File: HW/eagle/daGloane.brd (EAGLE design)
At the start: 182.4 x 160.7 mm, 64 parts, among them IC1 MCP1252-33X50, U1 STM32F10XTXU6, X2 SPARKFUN-CONNECTORS_USB-MICROB

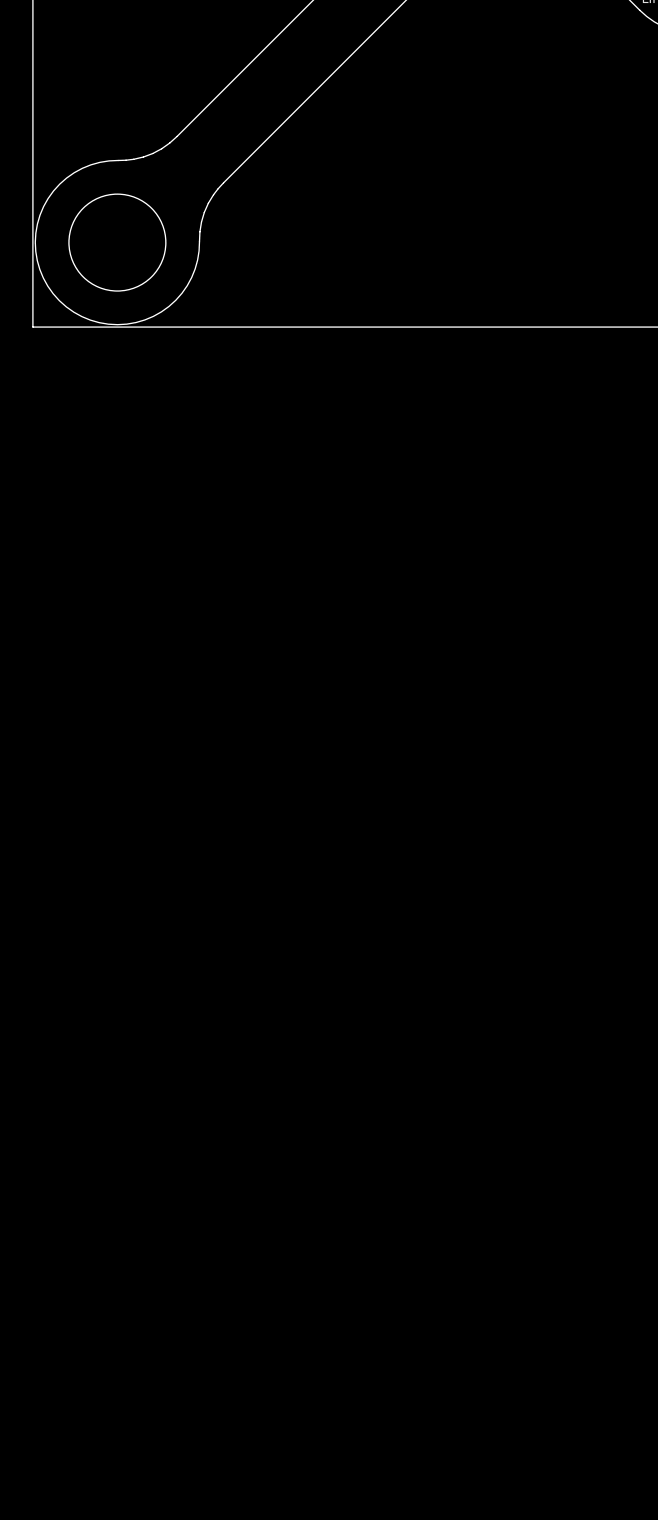
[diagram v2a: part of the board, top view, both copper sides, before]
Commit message: frame with bldc drive version added to schematic
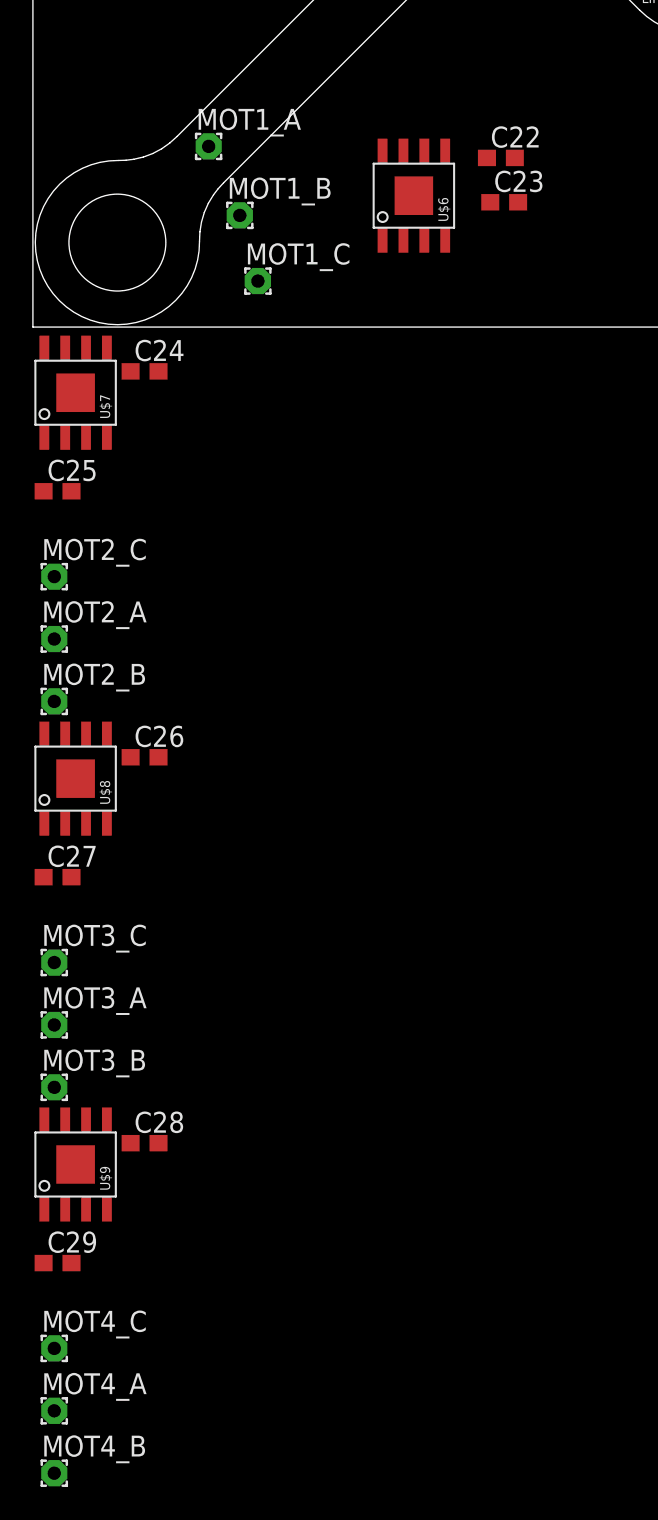
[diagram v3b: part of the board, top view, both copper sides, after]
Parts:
- added C22, C23, C24, C25, C26, C27, C28, C29: 1µF, rcl:C0603
- added MOT1_A, MOT1_B, MOT1_C, MOT2_A, MOT2_B, MOT2_C, MOT3_A, MOT3_B, MOT3_C, MOT4_A, MOT4_B, MOT4_C: WIREPAD1,6/0,8, wirepad:1,6/0,8
- added U$6, U$7, U$8, U$9: MTD6501C, daGloane:SOP-8
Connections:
- new net MOT1_A: MOT1_A.1, U$6.3
- new net MOT1_A1: MOT2_A.1, U$7.3
- new net MOT1_A2: MOT3_A.1, U$8.3
- new net MOT1_A3: MOT4_A.1, U$9.3
- new net N$26: C22.2, U$6.2
- new net N$27: MOT1_B.1, U$6.4
- new net N$29: MOT1_C.1, U$6.6
- new net N$30: MOT2_B.1, U$7.4
- new net N$31: MOT2_C.1, U$7.6
- new net N$32: C24.2, U$7.2
- new net N$33: MOT3_B.1, U$8.4
- new net N$34: MOT3_C.1, U$8.6
- new net N$35: C26.2, U$8.2
- new net N$36: MOT4_B.1, U$9.4
- new net N$37: MOT4_C.1, U$9.6
- new net N$38: C28.2, U$9.2
- new net V_MOT: C23.2, C25.2, C27.2, C29.2, U$6.7, U$7.7, U$8.7, U$9.7
- net GND: now also C22.1, C23.1, C24.1, C25.1, C26.1, C27.1, C28.1, C29.1, U$6.5, U$7.5, U$8.5, U$9.5
- net MOT1: now also U$6.8
- net MOT2: now also U$7.8
- net MOT3: now also U$8.8
- net MOT4: now also U$9.8
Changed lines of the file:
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@@
 <?xml version="1.0" encoding="utf-8"?>
 <!DOCTYPE eagle SYSTEM "eagle.dtd">
-<eagle version="6.2">
+<eagle version="6.1">
 <drawing>
 <settings>
@@
 <attribute name="VALUE" x="23.595" y="32.825" size="0.6096" layer="27"/>
 </element>
+<element name="U$6" library="daGloane" package="SOP-8" value="MTD6501C" x="23.2" y="8"/>
+<element name="C22" library="rcl" package="C0603" value="1µF" x="28.5" y="10.3"/>
+<element name="C23" library="rcl" package="C0603" value="1µF" x="28.7" y="7.6"/>
+<element name="MOT1_A" library="wirepad" package="1,6/0,8" value="WIREPAD1,6/0,8" x="10.7" y="11"/>
+<element name="MOT1_B" library="wirepad" package="1,6/0,8" value="WIREPAD1,6/0,8" x="12.6" y="6.8"/>
+<element name="MOT1_C" library="wirepad" package="1,6/0,8" value="WIREPAD1,6/0,8" x="13.7" y="2.8"/>
+<element name="U$7" library="daGloane" package="SOP-8" value="MTD6501C" x="2.6" y="-4"/>
+<element name="C24" library="rcl" package="C0603" value="1µF" x="6.8" y="-2.7"/>
+<element name="C25" library="rcl" package="C0603" value="1µF" x="1.5" y="-10"/>
+<element name="MOT2_A" library="wirepad" package="1,6/0,8" value="WIREPAD1,6/0,8" x="1.3" y="-19"/>
+<element name="MOT2_B" library="wirepad" package="1,6/0,8" value="WIREPAD1,6/0,8" x="1.3" y="-22.8"/>
+<element name="MOT2_C" library="wirepad" package="1,6/0,8" value="WIREPAD1,6/0,8" x="1.3" y="-15.2"/>
+<element name="U$8" library="daGloane" package="SOP-8" value="MTD6501C" x="2.6" y="-27.5"/>
+<element name="C26" library="rcl" package="C0603" value="1µF" x="6.8" y="-26.2"/>
+<element name="C27" library="rcl" package="C0603" value="1µF" x="1.5" y="-33.5"/>
+<element name="MOT3_A" library="wirepad" package="1,6/0,8" value="WIREPAD1,6/0,8" x="1.3" y="-42.5"/>
+<element name="MOT3_B" library="wirepad" package="1,6/0,8" value="WIREPAD1,6/0,8" x="1.3" y="-46.3"/>
+<element name="MOT3_C" library="wirepad" package="1,6/0,8" value="WIREPAD1,6/0,8" x="1.3" y="-38.7"/>
+<element name="U$9" library="daGloane" package="SOP-8" value="MTD6501C" x="2.6" y="-51"/>
+<element name="C28" library="rcl" package="C0603" value="1µF" x="6.8" y="-49.7"/>
+<element name="C29" library="rcl" package="C0603" value="1µF" x="1.5" y="-57"/>
+<element name="MOT4_A" library="wirepad" package="1,6/0,8" value="WIREPAD1,6/0,8" x="1.3" y="-66"/>
+<element name="MOT4_B" library="wirepad" package="1,6/0,8" value="WIREPAD1,6/0,8" x="1.3" y="-69.8"/>
+<element name="MOT4_C" library="wirepad" package="1,6/0,8" value="WIREPAD1,6/0,8" x="1.3" y="-62.2"/>
 </elements>
 <signals>
@@
 <contactref element="U$5" pad="P$22"/>
 <contactref element="C21" pad="2"/>
+<contactref element="U$6" pad="5"/>
+<contactref element="U$6" pad="5"/>
+<contactref element="C22" pad="1"/>
+<contactref element="C23" pad="1"/>
+<contactref element="U$7" pad="5"/>
+<contactref element="U$7" pad="5"/>
+<contactref element="C24" pad="1"/>
+<contactref element="C25" pad="1"/>
+<contactref element="U$8" pad="5"/>
+<contactref element="U$8" pad="5"/>
+<contactref element="C26" pad="1"/>
+<contactref element="C27" pad="1"/>
+<contactref element="U$9" pad="5"/>
+<contactref element="U$9" pad="5"/>
+<contactref element="C28" pad="1"/>
+<contactref element="C29" pad="1"/>
 <wire x1="91.72993125" y1="23.41184375" x2="94.367440625" y2="24.380578125" width="0" layer="19" extent="16-16"/>
 <wire x1="92.15419375" y1="21.99763125" x2="91.72993125" y2="23.41184375" width="0" layer="19" extent="16-16"/>
@@
 <wire x1="25.95" y1="62" x2="34.7" y2="55.2" width="0" layer="19" extent="1-1"/>
 <wire x1="25.95" y1="66" x2="25.95" y2="62" width="0" layer="19" extent="1-1"/>
+<wire x1="27.65" y1="10.3" x2="33.8" y2="27.55" width="0" layer="19" extent="1-1"/>
+<wire x1="25.105" y1="10.7" x2="27.65" y2="10.3" width="0" layer="19" extent="1-1"/>
+<wire x1="27.85" y1="7.6" x2="27.65" y2="10.3" width="0" layer="19" extent="1-1"/>
+<wire x1="5.95" y1="-2.7" x2="25.105" y2="10.7" width="0" layer="19" extent="1-1"/>
+<wire x1="4.505" y1="-1.3" x2="5.95" y2="-2.7" width="0" layer="19" extent="1-1"/>
+<wire x1="0.65" y1="-10" x2="5.95" y2="-2.7" width="0" layer="19" extent="1-1"/>
+<wire x1="4.505" y1="-24.8" x2="0.65" y2="-10" width="0" layer="19" extent="1-1"/>
+<wire x1="5.95" y1="-26.2" x2="4.505" y2="-24.8" width="0" layer="19" extent="1-1"/>
+<wire x1="0.65" y1="-33.5" x2="5.95" y2="-26.2" width="0" layer="19" extent="1-1"/>
+<wire x1="4.505" y1="-48.3" x2="0.65" y2="-33.5" width="0" layer="19" extent="1-1"/>
+<wire x1="5.95" y1="-49.7" x2="4.505" y2="-48.3" width="0" layer="19" extent="1-1"/>
+<wire x1="0.65" y1="-57" x2="5.95" y2="-49.7" width="0" layer="19" extent="1-1"/>
 </signal>
 <signal name="LED1">
@@
 <signal name="MOT4">
 <contactref element="U1" pad="32"/>
+<contactref element="U$9" pad="8"/>
+<wire x1="0.695" y1="-48.3" x2="40.5" y2="55.375" width="0" layer="19" extent="1-1"/>
 </signal>
 <signal name="N$1">
@@
 <signal name="MOT1">
 <contactref element="U1" pad="15"/>
+<contactref element="U$6" pad="8"/>
+<wire x1="21.295" y1="10.7" x2="41" y2="49.825" width="0" layer="19" extent="1-1"/>
 </signal>
 <signal name="MOT2">
 <contactref element="U1" pad="16"/>
+<contactref element="U$7" pad="8"/>
+<wire x1="0.695" y1="-1.3" x2="41.5" y2="49.825" width="0" layer="19" extent="1-1"/>
 </signal>
 <signal name="MOT3">
 <contactref element="U1" pad="31"/>
+<contactref element="U$8" pad="8"/>
+<wire x1="0.695" y1="-24.8" x2="41" y2="55.375" width="0" layer="19" extent="1-1"/>
+</signal>
+<signal name="MOT1_A">
+<contactref element="U$6" pad="3"/>
+<contactref element="MOT1_A" pad="1"/>
+<wire x1="23.835" y1="5.3" x2="10.7" y2="11" width="0" layer="19" extent="1-1"/>
+</signal>
+<signal name="N$27">
+<contactref element="U$6" pad="4"/>
+<contactref element="MOT1_B" pad="1"/>
+<wire x1="25.105" y1="5.3" x2="12.6" y2="6.8" width="0" layer="19" extent="1-1"/>
+</signal>
+<signal name="N$29">
+<contactref element="U$6" pad="6"/>
+<contactref element="MOT1_C" pad="1"/>
+<wire x1="23.835" y1="10.7" x2="13.7" y2="2.8" width="0" layer="19" extent="1-1"/>
+</signal>
+<signal name="N$26">
+<contactref element="U$6" pad="2"/>
+<contactref element="C22" pad="2"/>
+<wire x1="22.565" y1="5.3" x2="29.35" y2="10.3" width="0" layer="19" extent="1-1"/>
+</signal>
+<signal name="V_MOT">
+<contactref element="U$6" pad="7"/>
+<contactref element="C23" pad="2"/>
+<contactref element="U$7" pad="7"/>
+<contactref element="C25" pad="2"/>
+<contactref element="U$8" pad="7"/>
+<contactref element="C27" pad="2"/>
+<contactref element="U$9" pad="7"/>
+<contactref element="C29" pad="2"/>
+<wire x1="1.965" y1="-48.3" x2="2.35" y2="-57" width="0" layer="19" extent="1-1"/>
+<wire x1="2.35" y1="-33.5" x2="1.965" y2="-48.3" width="0" layer="19" extent="1-1"/>
+<wire x1="1.965" y1="-24.8" x2="2.35" y2="-33.5" width="0" layer="19" extent="1-1"/>
+<wire x1="2.35" y1="-10" x2="1.965" y2="-24.8" width="0" layer="19" extent="1-1"/>
+<wire x1="1.965" y1="-1.3" x2="2.35" y2="-10" width="0" layer="19" extent="1-1"/>
+<wire x1="22.565" y1="10.7" x2="1.965" y2="-1.3" width="0" layer="19" extent="1-1"/>
+<wire x1="29.55" y1="7.6" x2="22.565" y2="10.7" width="0" layer="19" extent="1-1"/>
+</signal>
+<signal name="MOT1_A1">
+<contactref element="U$7" pad="3"/>
+<contactref element="MOT2_A" pad="1"/>
+<wire x1="3.235" y1="-6.7" x2="1.3" y2="-19" width="0" layer="19" extent="1-1"/>
+</signal>
+<signal name="N$30">
+<contactref element="U$7" pad="4"/>
+<contactref element="MOT2_B" pad="1"/>
+<wire x1="4.505" y1="-6.7" x2="1.3" y2="-22.8" width="0" layer="19" extent="1-1"/>
+</signal>
+<signal name="N$31">
+<contactref element="U$7" pad="6"/>
+<contactref element="MOT2_C" pad="1"/>
+<wire x1="3.235" y1="-1.3" x2="1.3" y2="-15.2" width="0" layer="19" extent="1-1"/>
+</signal>
+<signal name="N$32">
+<contactref element="U$7" pad="2"/>
+<contactref element="C24" pad="2"/>
+<wire x1="7.65" y1="-2.7" x2="1.965" y2="-6.7" width="0" layer="19" extent="1-1"/>
+</signal>
+<signal name="MOT1_A2">
+<contactref element="U$8" pad="3"/>
+<contactref element="MOT3_A" pad="1"/>
+<wire x1="3.235" y1="-30.2" x2="1.3" y2="-42.5" width="0" layer="19" extent="1-1"/>
+</signal>
+<signal name="N$33">
+<contactref element="U$8" pad="4"/>
+<contactref element="MOT3_B" pad="1"/>
+<wire x1="4.505" y1="-30.2" x2="1.3" y2="-46.3" width="0" layer="19" extent="1-1"/>
+</signal>
+<signal name="N$34">
+<contactref element="U$8" pad="6"/>
+<contactref element="MOT3_C" pad="1"/>
+<wire x1="3.235" y1="-24.8" x2="1.3" y2="-38.7" width="0" layer="19" extent="1-1"/>
+</signal>
+<signal name="N$35">
+<contactref element="U$8" pad="2"/>
+<contactref element="C26" pad="2"/>
+<wire x1="7.65" y1="-26.2" x2="1.965" y2="-30.2" width="0" layer="19" extent="1-1"/>
+</signal>
+<signal name="MOT1_A3">
+<contactref element="U$9" pad="3"/>
+<contactref element="MOT4_A" pad="1"/>
+<wire x1="3.235" y1="-53.7" x2="1.3" y2="-66" width="0" layer="19" extent="1-1"/>
+</signal>
+<signal name="N$36">
+<contactref element="U$9" pad="4"/>
+<contactref element="MOT4_B" pad="1"/>
+<wire x1="4.505" y1="-53.7" x2="1.3" y2="-69.8" width="0" layer="19" extent="1-1"/>
+</signal>
+<signal name="N$37">
+<contactref element="U$9" pad="6"/>
+<contactref element="MOT4_C" pad="1"/>
+<wire x1="3.235" y1="-48.3" x2="1.3" y2="-62.2" width="0" layer="19" extent="1-1"/>
+</signal>
+<signal name="N$38">
+<contactref element="U$9" pad="2"/>
+<contactref element="C28" pad="2"/>
+<wire x1="7.65" y1="-49.7" x2="1.965" y2="-53.7" width="0" layer="19" extent="1-1"/>
 </signal>
 </signals>

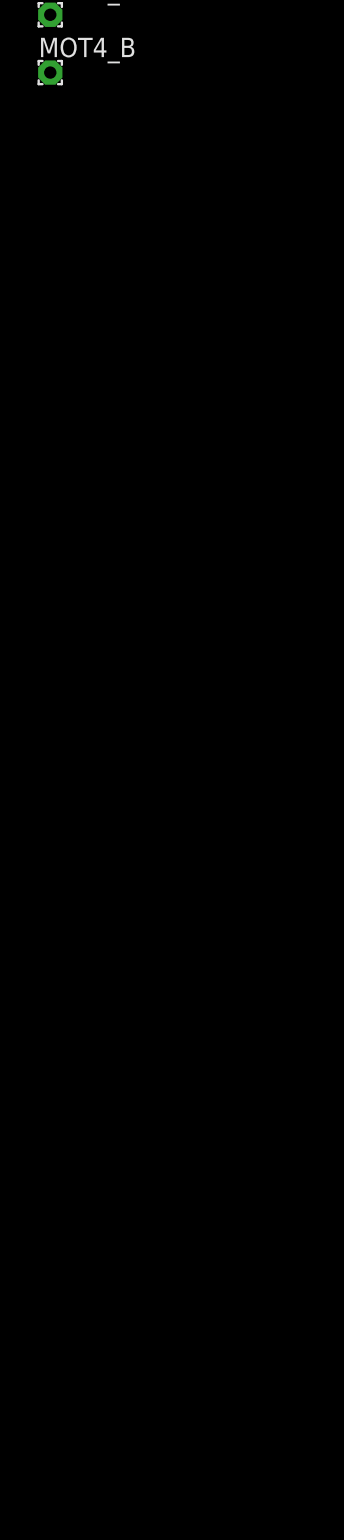
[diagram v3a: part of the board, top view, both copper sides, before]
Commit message: DC motor drive added to schematic
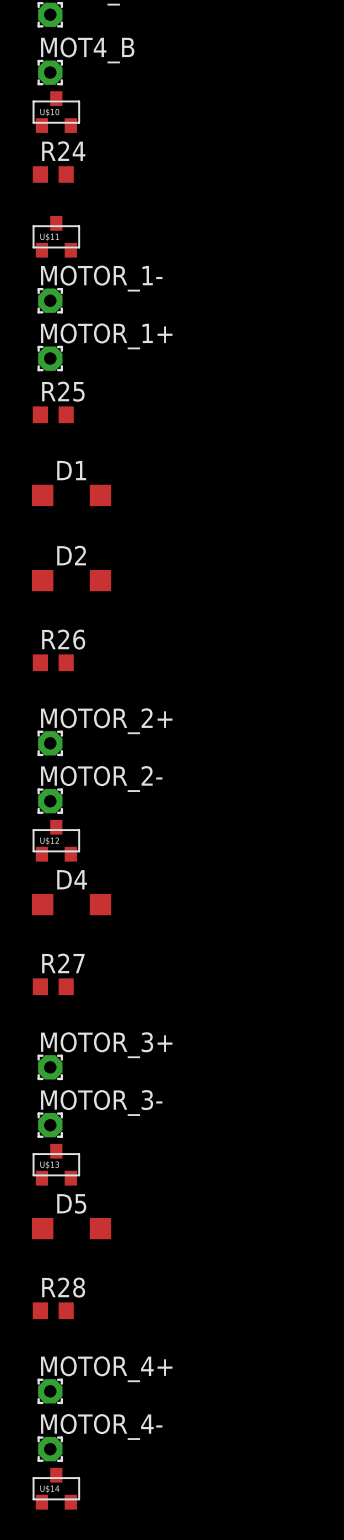
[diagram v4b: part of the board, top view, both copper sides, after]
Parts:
- added D1, D2, D4, D5: MBR0520LT, diode:SOD123
- added MOTOR_1+, MOTOR_1-, MOTOR_2+, MOTOR_2-, MOTOR_3+, MOTOR_3-, MOTOR_4+, MOTOR_4-: WIREPAD1,6/0,8, wirepad:1,6/0,8
- added R24, R25, R26, R27, R28: 10k, rcl:R0603
- added U$10, U$11, U$12, U$13, U$14: IRLM6344TRPBF, daGloane:MICRO3(SOT-23)
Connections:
- removed net V_MOT: C23.2, C25.2, C27.2, C29.2, U$6.7, U$7.7, U$8.7, U$9.7
- new net MOT_GND: C22.1, C24.1, C26.1, C28.1, U$10.3, U$6.5, U$7.5, U$8.5, U$9.5
- new net N$39: D1.A, MOTOR_1-.1, U$11.3
- new net N$40: D2.A, MOTOR_2-.1, U$12.3
- new net N$41: D4.A, MOTOR_3-.1, U$13.3
- new net N$42: D5.A, MOTOR_4-.1, U$14.3
- net GND: now also R24.1, R25.2, R26.2, R27.2, R28.2, U$10.2, U$11.2, U$12.2, U$13.2, U$14.2; no longer C22.1, C24.1, C26.1, C28.1, U$6.5, U$7.5, U$8.5, U$9.5
- net LIPO: now also C23.2, C25.2, C27.2, C29.2, D1.C, D2.C, D4.C, D5.C, MOTOR_1+.1, MOTOR_2+.1, MOTOR_3+.1, MOTOR_4+.1, U$6.7, U$7.7, U$8.7, U$9.7
- net MOT1: now also R25.1, U$11.1
- net MOT2: now also R26.1, U$12.1
- net MOT3: now also R27.1, U$13.1
- net MOT4: now also R28.1, U$14.1
- net VCC: now also R24.2, U$10.1

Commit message: gnd connection of decoppling capacitors of BLDC motor drivers changed to mot_gnd
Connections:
- net GND: no longer C23.1, C25.1, C27.1, C29.1
- net MOT_GND: now also C23.1, C25.1, C27.1, C29.1
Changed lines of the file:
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@@
 <?xml version="1.0" encoding="utf-8"?>
 <!DOCTYPE eagle SYSTEM "eagle.dtd">
-<eagle version="6.1">
+<eagle version="6.2">
 <drawing>
 <settings>
@@
 <contactref element="U$5" pad="P$22"/>
 <contactref element="C21" pad="2"/>
-<contactref element="C23" pad="1"/>
-<contactref element="C25" pad="1"/>
-<contactref element="C27" pad="1"/>
-<contactref element="C29" pad="1"/>
 <contactref element="U$10" pad="2"/>
 <contactref element="R24" pad="1"/>
@@
 <wire x1="0.65" y1="-76.5" x2="2.65" y2="-81.485" width="0" layer="19" extent="1-1"/>
 <wire x1="2.65" y1="-73.285" x2="0.65" y2="-76.5" width="0" layer="19" extent="1-1"/>
-<wire x1="0.65" y1="-57" x2="2.65" y2="-73.285" width="0" layer="19" extent="1-1"/>
-<wire x1="0.65" y1="-33.5" x2="0.65" y2="-57" width="0" layer="19" extent="1-1"/>
-<wire x1="0.65" y1="-10" x2="0.65" y2="-33.5" width="0" layer="19" extent="1-1"/>
-<wire x1="27.85" y1="7.6" x2="0.65" y2="-10" width="0" layer="19" extent="1-1"/>
-<wire x1="33.8" y1="27.55" x2="27.85" y2="7.6" width="0" layer="19" extent="1-1"/>
-<wire x1="35.45" y1="29.025" x2="33.8" y2="27.55" width="0" layer="19" extent="1-1"/>
-<wire x1="36.05" y1="27.5" x2="35.45" y2="29.025" width="0" layer="19" extent="1-1"/>
+<wire x1="43" y1="22.5" x2="2.65" y2="-73.285" width="0" layer="19" extent="1-1"/>
+<wire x1="45.15" y1="25.5" x2="43" y2="22.5" width="0" layer="19" extent="1-1"/>
+<wire x1="43.5" y1="28.15" x2="45.15" y2="25.5" width="0" layer="19" extent="1-1"/>
+<wire x1="46" y1="29.8001" x2="43.5" y2="28.15" width="0" layer="19" extent="1-1"/>
+<wire x1="48.5" y1="28.15" x2="46" y2="29.8001" width="0" layer="19" extent="1-1"/>
+<wire x1="36.05" y1="27.5" x2="43.5" y2="28.15" width="0" layer="19" extent="1-1"/>
+<wire x1="35.45" y1="29.025" x2="36.05" y2="27.5" width="0" layer="19" extent="1-1"/>
+<wire x1="33.8" y1="27.55" x2="35.45" y2="29.025" width="0" layer="19" extent="1-1"/>
 <wire x1="30.6" y1="32.15" x2="33.8" y2="27.55" width="0" layer="19" extent="1-1"/>
 <wire x1="28.5" y1="32.15" x2="30.6" y2="32.15" width="0" layer="19" extent="1-1"/>
 <wire x1="29.35" y1="39" x2="28.5" y2="32.15" width="0" layer="19" extent="1-1"/>
 <wire x1="29.35" y1="41.1" x2="29.35" y2="39" width="0" layer="19" extent="1-1"/>
-<wire x1="43.5" y1="28.15" x2="36.05" y2="27.5" width="0" layer="19" extent="1-1"/>
-<wire x1="46" y1="29.8001" x2="43.5" y2="28.15" width="0" layer="19" extent="1-1"/>
-<wire x1="48.5" y1="28.15" x2="46" y2="29.8001" width="0" layer="19" extent="1-1"/>
-<wire x1="45.15" y1="25.5" x2="43.5" y2="28.15" width="0" layer="19" extent="1-1"/>
-<wire x1="43" y1="22.5" x2="45.15" y2="25.5" width="0" layer="19" extent="1-1"/>
 <wire x1="37" y1="38.15" x2="29.35" y2="39" width="0" layer="19" extent="1-1"/>
 <wire x1="38.575" y1="39.25" x2="37" y2="38.15" width="0" layer="19" extent="1-1"/>
@@
 <contactref element="C28" pad="1"/>
 <contactref element="U$10" pad="3"/>
-<wire x1="5.95" y1="-49.7" x2="1.7" y2="-71.515" width="0" layer="19" extent="1-1"/>
+<contactref element="C23" pad="1"/>
+<contactref element="C25" pad="1"/>
+<contactref element="C29" pad="1"/>
+<contactref element="C27" pad="1"/>
+<wire x1="0.65" y1="-57" x2="1.7" y2="-71.515" width="0" layer="19" extent="1-1"/>
+<wire x1="5.95" y1="-49.7" x2="0.65" y2="-57" width="0" layer="19" extent="1-1"/>
 <wire x1="4.505" y1="-48.3" x2="5.95" y2="-49.7" width="0" layer="19" extent="1-1"/>
-<wire x1="5.95" y1="-26.2" x2="4.505" y2="-48.3" width="0" layer="19" extent="1-1"/>
+<wire x1="0.65" y1="-33.5" x2="4.505" y2="-48.3" width="0" layer="19" extent="1-1"/>
+<wire x1="5.95" y1="-26.2" x2="0.65" y2="-33.5" width="0" layer="19" extent="1-1"/>
 <wire x1="4.505" y1="-24.8" x2="5.95" y2="-26.2" width="0" layer="19" extent="1-1"/>
-<wire x1="5.95" y1="-2.7" x2="4.505" y2="-24.8" width="0" layer="19" extent="1-1"/>
+<wire x1="0.65" y1="-10" x2="4.505" y2="-24.8" width="0" layer="19" extent="1-1"/>
+<wire x1="5.95" y1="-2.7" x2="0.65" y2="-10" width="0" layer="19" extent="1-1"/>
 <wire x1="4.505" y1="-1.3" x2="5.95" y2="-2.7" width="0" layer="19" extent="1-1"/>
 <wire x1="25.105" y1="10.7" x2="5.95" y2="-2.7" width="0" layer="19" extent="1-1"/>
 <wire x1="27.65" y1="10.3" x2="25.105" y2="10.7" width="0" layer="19" extent="1-1"/>
+<wire x1="27.85" y1="7.6" x2="27.65" y2="10.3" width="0" layer="19" extent="1-1"/>
 </signal>
 <signal name="N$39">
